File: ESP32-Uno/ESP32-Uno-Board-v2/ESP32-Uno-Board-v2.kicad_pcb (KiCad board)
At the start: 2 copper layers, 68.8 x 53.2 mm, 19 parts, among them J1 USB-C_Receptacle_Data_16P_GCT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, J2 Barrel_Jack_Switch, Q1 DMP6180SK3, SW1 SW_SPDT, SW2 SW_Push_SMD_6x3.5, U1 ESP32-S3-WROOM-1, U2 LM1117MP-3.3, U3 AMS1117-5V

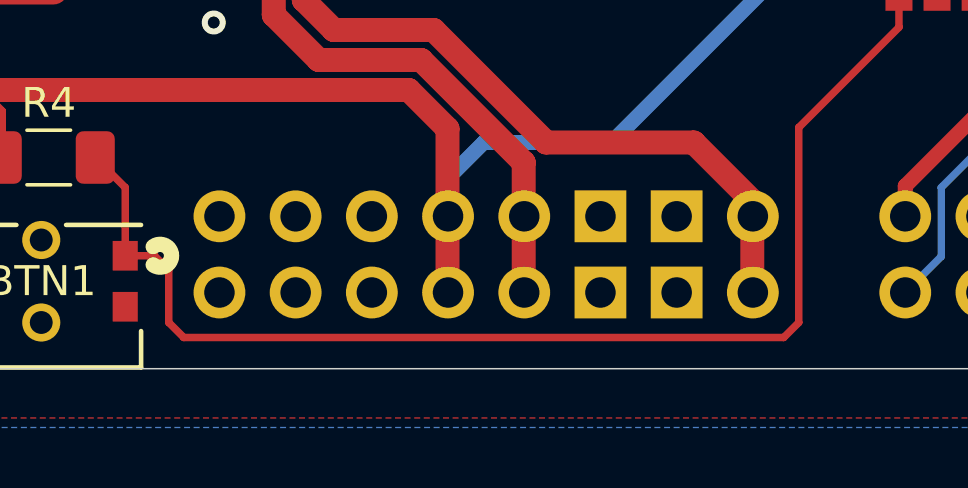
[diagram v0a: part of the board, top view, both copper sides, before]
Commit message: ESP32-Uno
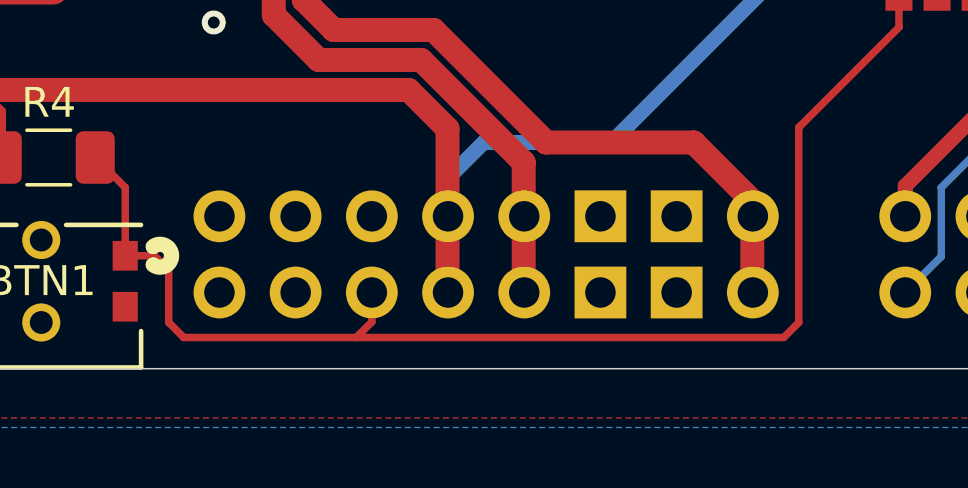
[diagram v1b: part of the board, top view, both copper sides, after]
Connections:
- A2 pad RST1: unconnected-(A2-RESET-PadRST1) -> /GPIO0
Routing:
- net /GPIO0: track 41.0 -> 42.7 mm

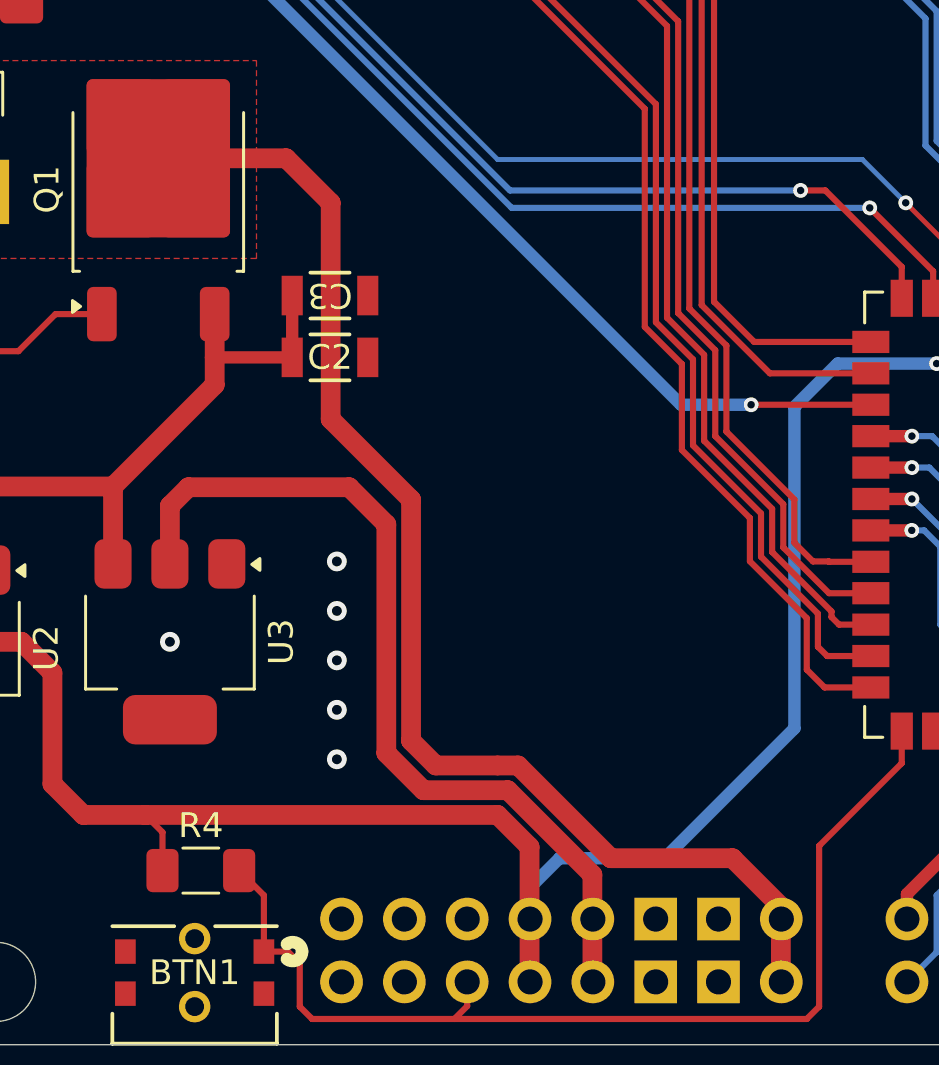
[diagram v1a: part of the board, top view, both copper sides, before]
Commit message: ESP32-Uno
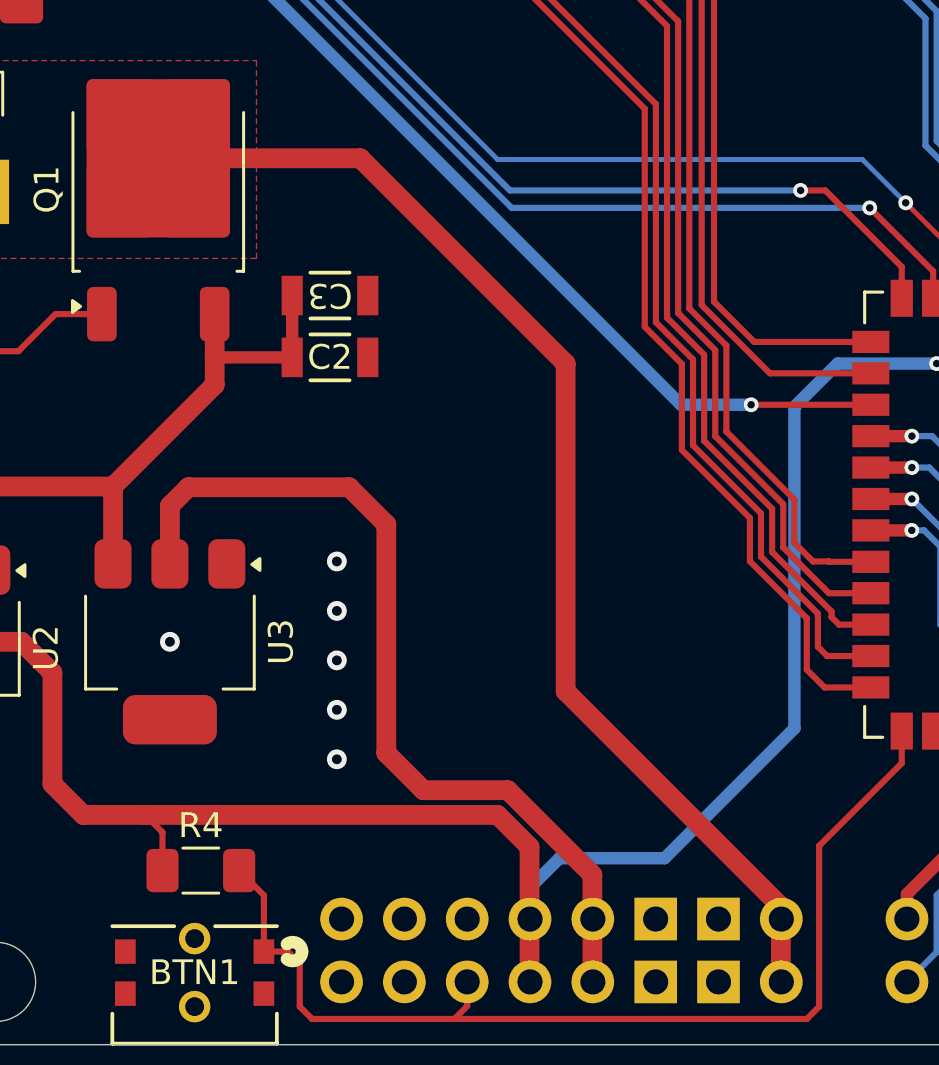
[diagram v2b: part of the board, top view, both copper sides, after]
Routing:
- net VIN: track 51.7 -> 48.6 mm
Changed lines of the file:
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@@
-	)
-	(segment
-		(start 135.7 116.95)
-		(end 137.5 118.75)
-		(width 0.8)
-		(layer "F.Cu")
-		(net 43)
-	)
-	(segment
-		(start 137.5 118.75)
-		(end 137.5 127.5)
-		(width 0.8)
-		(layer "F.Cu")
-		(net 43)
-	)
-	(segment
-		(start 137.5 127.5)
-		(end 140.75 130.75)
-		(width 0.8)
-		(layer "F.Cu")
-		(net 43)
-	)
-	(segment
-		(start 140.75 140.5)
-		(end 141.75 141.5)
-		(width 0.8)
-		(layer "F.Cu")
-		(net 43)
 	)
 	(segment
@@
 	)
 	(segment
-		(start 140.75 130.75)
-		(end 140.75 140.5)
+		(start 138.7 116.95)
+		(end 147 125.25)
+		(width 0.8)
+		(layer "F.Cu")
+		(net 43)
+	)
+	(segment
+		(start 147 138.5)
+		(end 155.702 147.202)
 		(width 0.8)
 		(layer "F.Cu")
@@
 	(segment
 		(start 130.53 116.95)
-		(end 135.7 116.95)
+		(end 138.7 116.95)
 		(width 0.8)
 		(layer "F.Cu")
@@
 	)
 	(segment
-		(start 141.75 141.5)
-		(end 144.250001 141.499999)
+		(start 147 125.25)
+		(end 147 138.5)
 		(width 0.8)
 		(layer "F.Cu")
-		(net 43)
-	)
-	(segment
-		(start 148.828428 145.25)
-		(end 153.75 145.25)
-		(width 0.8)
-		(layer "F.Cu")
-		(net 43)
-	)
-	(segment
-		(start 144.250001 141.499999)
-		(end 145.078427 141.499999)
-		(width 0.8)
-		(layer "F.Cu")
-		(net 43)
-	)
-	(segment
-		(start 153.75 145.25)
-		(end 155.702 147.202)
-		(width 0.8)
-		(layer "F.Cu")
-		(net 43)
-	)
-	(segment
-		(start 145.078427 141.499999)
-		(end 148.828428 145.25)
-		(width 0.8)
-		(layer "F.Cu")

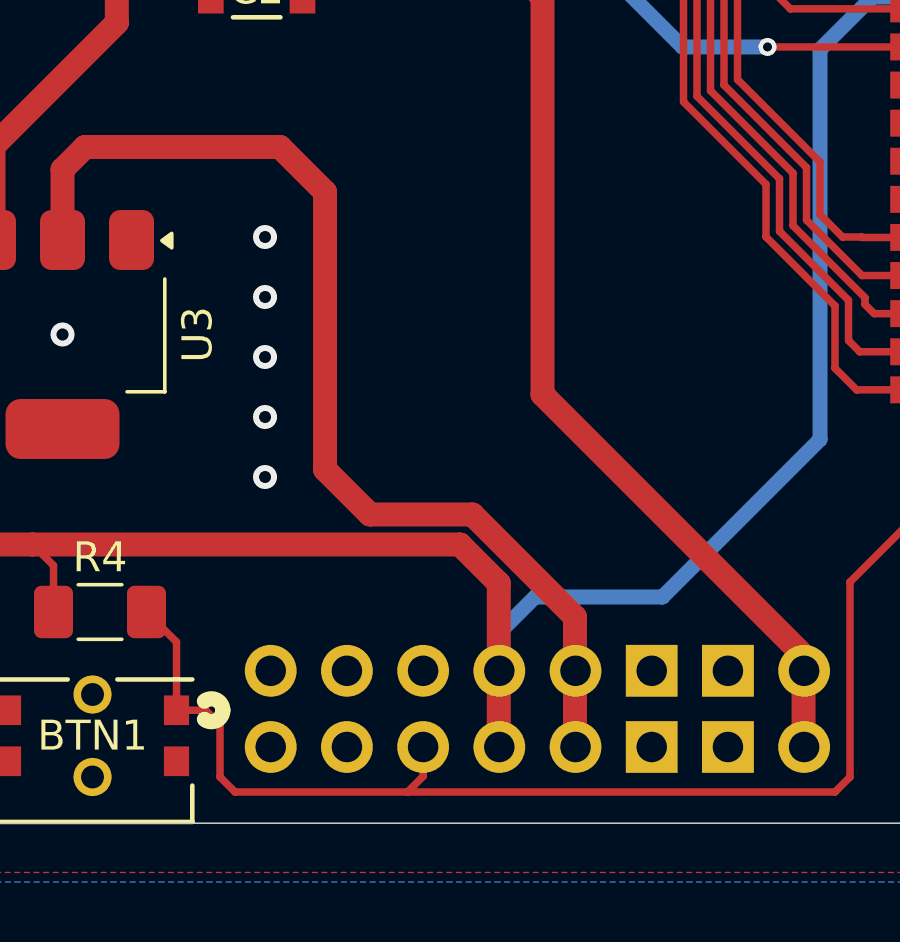
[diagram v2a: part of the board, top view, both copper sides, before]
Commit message: ESP32-Uno
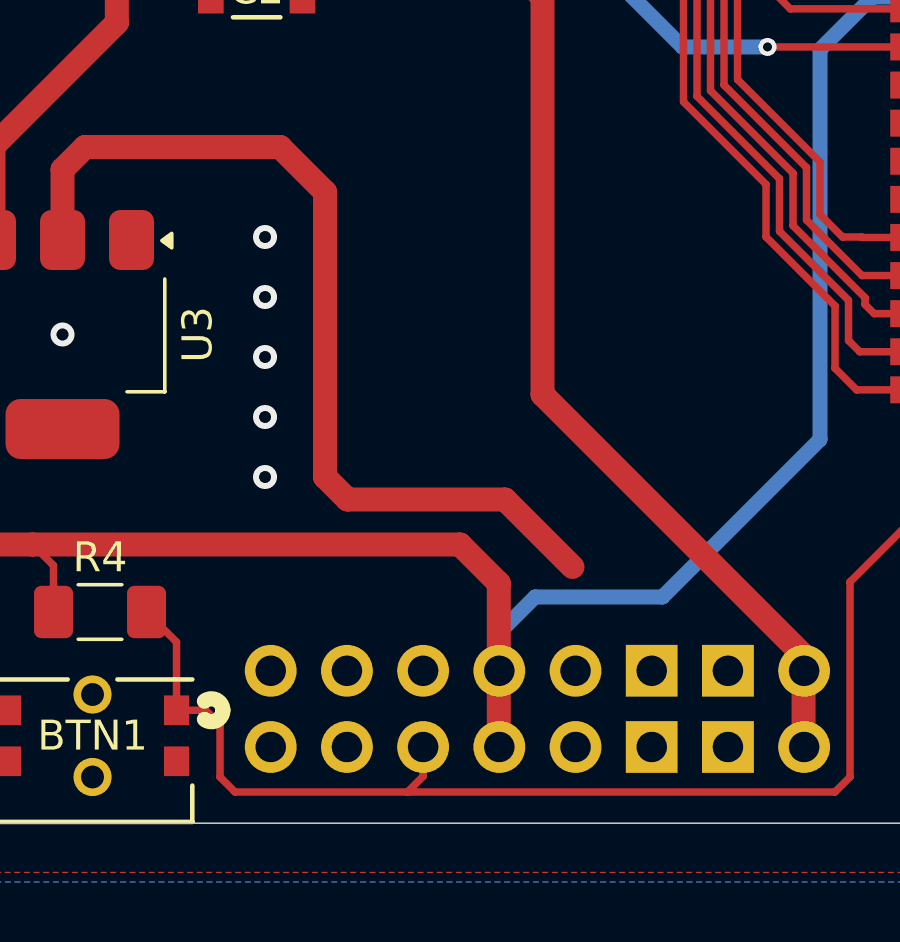
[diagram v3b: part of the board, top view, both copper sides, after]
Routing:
- net +5V: track 36.1 -> 31.0 mm
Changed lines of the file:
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@@
 	)
 	(segment
-		(start 139.75 131.75)
-		(end 139.75 141)
+		(start 138.25 130.25)
+		(end 139.75 131.75)
 		(width 0.8)
 		(layer "F.Cu")
@@
 	)
 	(segment
-		(start 138.25 130.25)
-		(end 139.75 131.75)
+		(start 140.5 142)
+		(end 145.75 142)
+		(width 0.8)
+		(layer "F.Cu")
+		(net 1)
+	)
+	(segment
+		(start 139.75 141.25)
+		(end 140.5 142)
 		(width 0.8)
 		(layer "F.Cu")
@@
 	)
 	(segment
-		(start 139.75 141)
-		(end 141.25 142.5)
+		(start 145.75 142)
+		(end 148 144.25)
 		(width 0.8)
 		(layer "F.Cu")
@@
 	)
 	(segment
-		(start 141.25 142.5)
-		(end 144.664214 142.5)
+		(start 139.75 131.75)
+		(end 139.75 141.25)
 		(width 0.8)
 		(layer "F.Cu")
-		(net 1)
-	)
-	(segment
-		(start 148.082 145.917786)
-		(end 148.082 150.368)
-		(width 0.8)
-		(layer "F.Cu")
-		(net 1)
-	)
-	(segment
-		(start 144.664214 142.5)
-		(end 148.082 145.917786)
-		(width 0.8)
-		(layer "F.Cu")

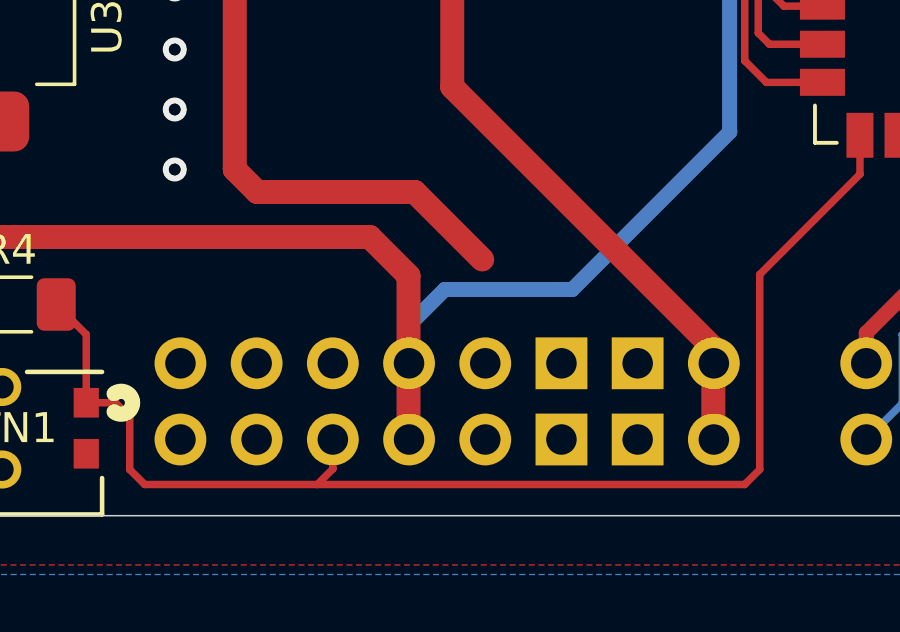
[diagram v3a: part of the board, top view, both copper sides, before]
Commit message: ESP32-Uno
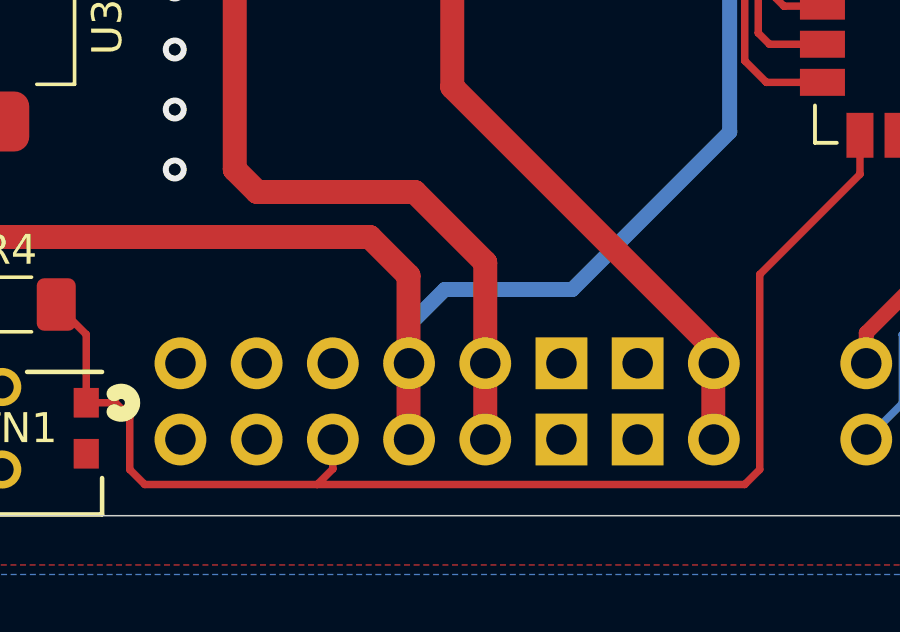
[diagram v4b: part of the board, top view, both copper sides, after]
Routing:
- net +5V: track 31.0 -> 37.1 mm

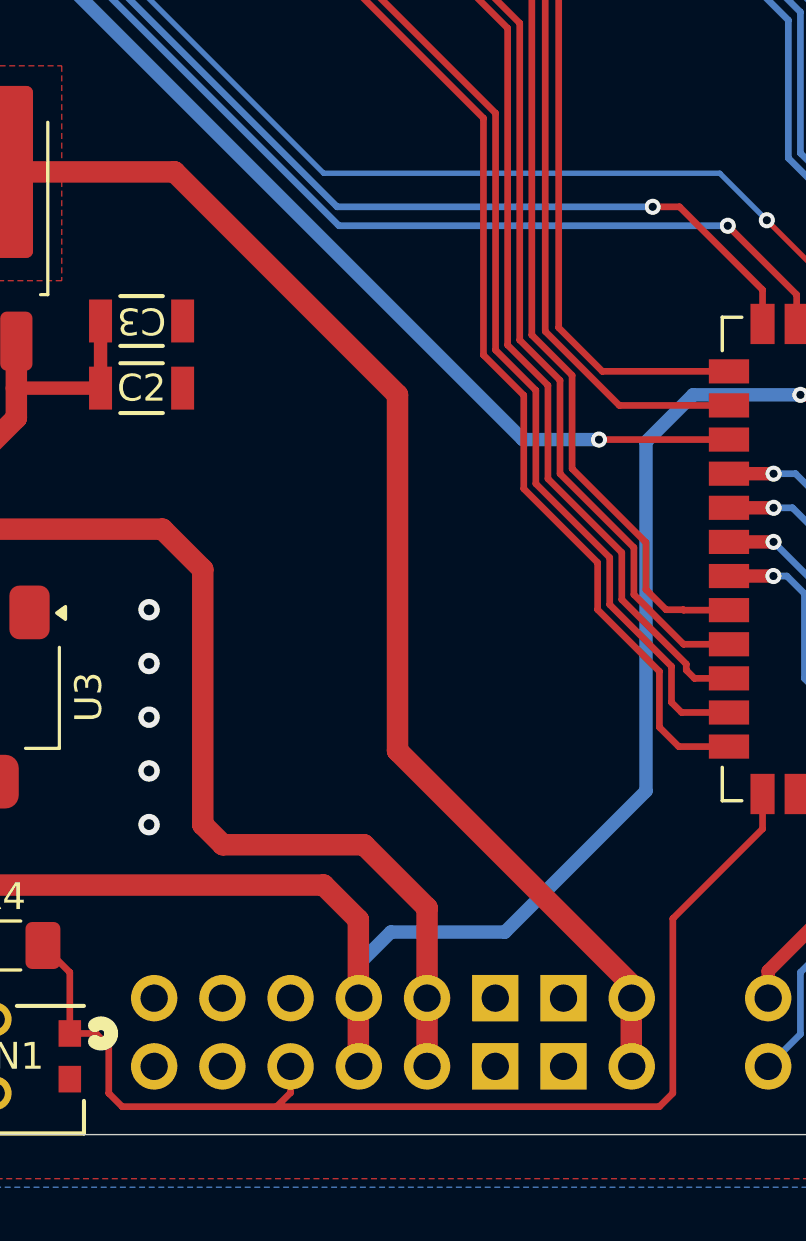
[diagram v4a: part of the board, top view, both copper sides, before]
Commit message: ESP32-Uno
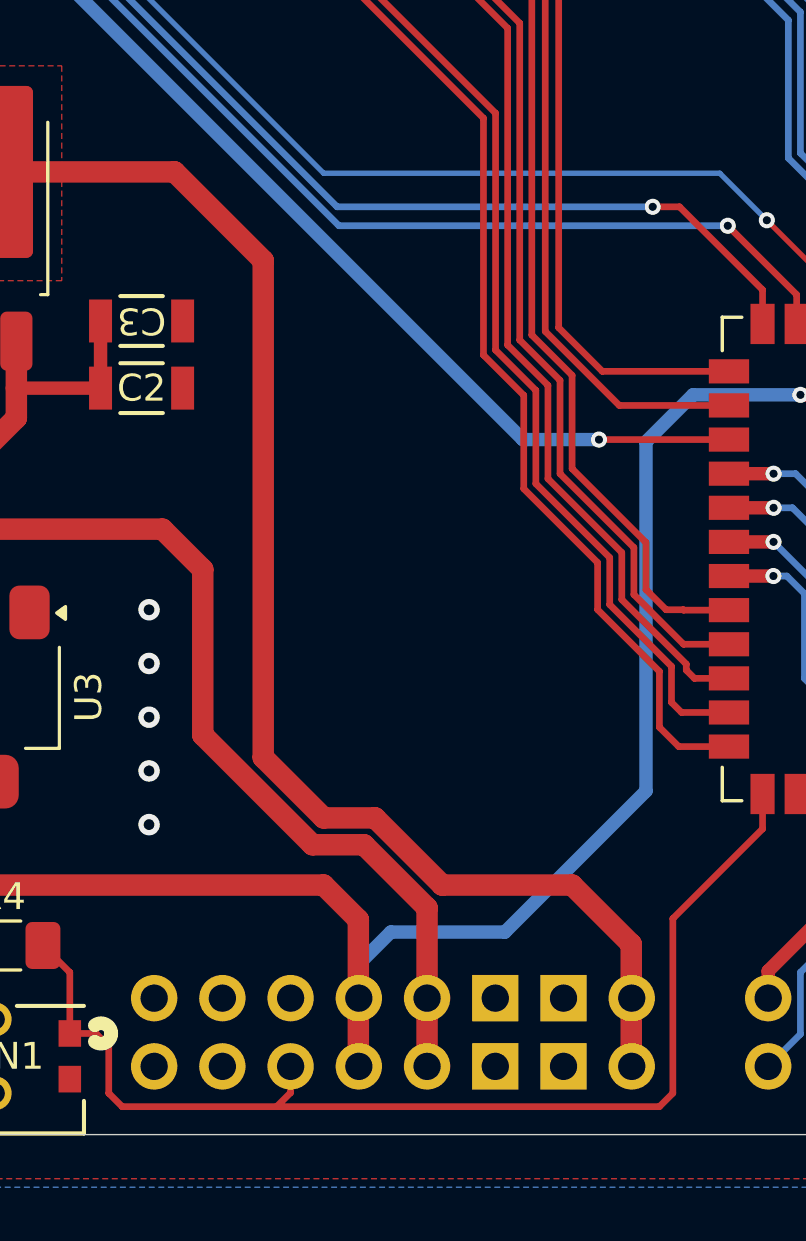
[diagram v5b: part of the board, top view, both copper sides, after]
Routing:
- net VIN: track 48.6 -> 52.6 mm
- net +5V: track 37.1 -> 35.1 mm
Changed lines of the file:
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@@
 	)
 	(segment
-		(start 139.75 141.25)
-		(end 140.5 142)
+		(start 148.1 144.35)
+		(end 148.1 147.71)
+		(width 0.8)
+		(layer "F.Cu")
+		(net 1)
+	)
+	(segment
+		(start 145.75 142)
+		(end 148.1 144.35)
 		(width 0.8)
 		(layer "F.Cu")
@@
 	)
 	(segment
+		(start 138.25 130.25)
+		(end 139.75 131.75)
+		(width 0.8)
+		(layer "F.Cu")
+		(net 1)
+	)
+	(segment
 		(start 148.1 147.71)
 		(end 148.1 150.25)
@@
 	)
 	(segment
-		(start 138.25 130.25)
-		(end 139.75 131.75)
+		(start 143.835786 142)
+		(end 145.75 142)
+		(width 0.8)
+		(layer "F.Cu")
+		(net 1)
+	)
+	(segment
+		(start 131 131)
+		(end 131.75 130.25)
+		(width 0.8)
+		(layer "F.Cu")
+		(net 1)
+	)
+	(segment
+		(start 139.75 137.914214)
+		(end 143.835786 142)
+		(width 0.8)
+		(layer "F.Cu")
+		(net 1)
+	)
+	(segment
+		(start 139.75 131.75)
+		(end 139.75 137.914214)
 		(width 0.8)
 		(layer "F.Cu")
@@
 		(start 131.75 130.25)
 		(end 138.25 130.25)
-		(width 0.8)
-		(layer "F.Cu")
-		(net 1)
-	)
-	(segment
-		(start 148.1 144.35)
-		(end 148.1 147.71)
-		(width 0.8)
-		(layer "F.Cu")
-		(net 1)
-	)
-	(segment
-		(start 140.5 142)
-		(end 145.75 142)
-		(width 0.8)
-		(layer "F.Cu")
-		(net 1)
-	)
-	(segment
-		(start 139.75 131.75)
-		(end 139.75 141.25)
-		(width 0.8)
-		(layer "F.Cu")
-		(net 1)
-	)
-	(segment
-		(start 145.75 142)
-		(end 148.1 144.35)
-		(width 0.8)
-		(layer "F.Cu")
-		(net 1)
-	)
-	(segment
-		(start 131 131)
-		(end 131.75 130.25)
 		(width 0.8)
 		(layer "F.Cu")
@@
 	)
 	(segment
-		(start 155.702 147.202)
-		(end 155.702 150.368)
+		(start 153.5 143.5)
+		(end 155.702 145.702)
 		(width 0.8)
 		(layer "F.Cu")
@@
 	(segment
 		(start 138.7 116.95)
-		(end 147 125.25)
-		(width 0.8)
-		(layer "F.Cu")
-		(net 43)
-	)
-	(segment
-		(start 147 138.5)
-		(end 155.702 147.202)
+		(end 142 120.25)
 		(width 0.8)
 		(layer "F.Cu")
@@
 	)
 	(segment
-		(start 147 125.25)
-		(end 147 138.5)
-		(width 0.8)
-		(layer "F.Cu")
+		(start 142 138.75)
+		(end 144.25 141)
+		(width 0.8)
+		(layer "F.Cu")
+		(net 43)
+	)
+	(segment
+		(start 142 120.25)
+		(end 142 138.75)
+		(width 0.8)
+		(layer "F.Cu")
+		(net 43)
+	)
+	(segment
+		(start 144.25 141)
+		(end 146.164214 141)
+		(width 0.8)
+		(layer "F.Cu")
+		(net 43)
+	)
+	(segment
+		(start 146.164214 141)
+		(end 148.664214 143.5)
+		(width 0.8)
+		(layer "F.Cu")
+		(net 43)
+	)
+	(segment
+		(start 155.702 145.702)
+		(end 155.702 150.368)
+		(width 0.8)
+		(layer "F.Cu")
+		(net 43)
+	)
+	(segment
+		(start 148.664214 143.5)
+		(end 153.5 143.5)
+		(width 0.8)
+		(layer "F.Cu")
